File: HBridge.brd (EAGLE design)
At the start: 59.7 x 53.3 mm, 51 parts, among them IC1 74LS08D, IC2 A4954, J1 Inputs, J11 PWM mode, J12 Fixed mode, J13 Ground, J14 5V, J15 Digital_8_13, J16 Analog, J17 Digital_0_7, J4 PWM mode, J5 Fixed mode, J6 Power, J7 Output A, J8 Output B

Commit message: foo
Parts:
- moved J1 2.54 mm to (38.1, 36.8)
- moved C4 1.91 mm to (34.9, 21.6)
- moved R8 1.91 mm to (34.9, 19.7)
- moved R3 0.63 mm to (34.9, 23.5)
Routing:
- net IN4: track 18.3 -> 20.9 mm
- net PWM34: track 28.7 -> 29.8 mm
- net PWM12: track 31.7 -> 32.7 mm
- net IN2: track 24.1 -> 25.2 mm
- net IN1: track 23.6 -> 24.6 mm
- net REF_PWM_12: track 2.41 -> 3.20 mm
- net N$19: track 3.81 -> 4.45 mm

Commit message: foo
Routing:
- net N$66: track 11.4 -> 9.24 mm
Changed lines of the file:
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@@
 <wire x1="32.7025" y1="35.4965" x2="32.385" y2="35.814" width="0.4064" layer="1"/>
 <wire x1="32.385" y1="35.814" x2="32.385" y2="37.465" width="0.4064" layer="1"/>
-<wire x1="32.7025" y1="34.6075" x2="32.7025" y2="32.7025" width="0.3048" layer="16"/>
-<wire x1="32.7025" y1="32.7025" x2="31.75" y2="31.75" width="0.3048" layer="16"/>
-<wire x1="31.75" y1="31.75" x2="30.48" y2="31.75" width="0.3048" layer="16"/>
+<wire x1="32.7025" y1="34.6075" x2="32.7025" y2="32.7025" width="0.4064" layer="16"/>
+<wire x1="32.7025" y1="32.7025" x2="31.75" y2="31.75" width="0.4064" layer="16"/>
+<wire x1="31.75" y1="31.75" x2="30.48" y2="31.75" width="0.4064" layer="16"/>
 </signal>
 <signal name="N$17">
@@
 <wire x1="18.415" y1="34.29" x2="19.685" y2="35.56" width="0.4064" layer="1"/>
 <via x="19.685" y="35.56" extent="1-16" drill="0.4"/>
-<wire x1="38.1" y1="34.29" x2="34.29" y2="38.1" width="0.2032" layer="16"/>
-<wire x1="34.29" y1="38.1" x2="22.225" y2="38.1" width="0.2032" layer="16"/>
-<wire x1="22.225" y1="38.1" x2="19.685" y2="35.56" width="0.2032" layer="16"/>
+<wire x1="38.1" y1="34.29" x2="34.29" y2="38.1" width="0.4064" layer="16"/>
+<wire x1="31.115" y1="38.1" x2="27.305" y2="38.1" width="0.2032" layer="16"/>
+<wire x1="19.685" y1="35.56" x2="22.225" y2="38.1" width="0.4064" layer="16"/>
+<wire x1="22.225" y1="38.1" x2="27.305" y2="38.1" width="0.4064" layer="16"/>
+<wire x1="31.115" y1="38.1" x2="34.29" y2="38.1" width="0.4064" layer="16"/>
 </signal>
 <signal name="IN1">
@@
 <wire x1="22.86" y1="41.402" x2="32.258" y2="41.402" width="0.4064" layer="1"/>
 <wire x1="32.258" y1="41.402" x2="33.655" y2="40.005" width="0.4064" layer="1"/>
-<wire x1="38.1" y1="41.91" x2="40.64" y2="41.91" width="0.4064" layer="1"/>
+<wire x1="38.1" y1="41.91" x2="40.64" y2="41.91" width="0.8128" layer="1"/>
 <wire x1="48.26" y1="41.91" x2="50.8" y2="41.91" width="0.2032" layer="1"/>
 <wire x1="50.8" y1="41.91" x2="53.34" y2="41.91" width="0.4064" layer="1"/>
 <wire x1="53.34" y1="41.91" x2="55.88" y2="41.91" width="0.4064" layer="1"/>
-<wire x1="55.88" y1="41.91" x2="48.26" y2="41.91" width="0.4064" layer="1"/>
-<wire x1="48.26" y1="41.91" x2="45.72" y2="41.91" width="0.4064" layer="1"/>
-<wire x1="45.72" y1="41.91" x2="43.18" y2="41.91" width="0.4064" layer="1"/>
-<wire x1="43.18" y1="41.91" x2="40.64" y2="41.91" width="0.4064" layer="1"/>
+<wire x1="55.88" y1="41.91" x2="48.26" y2="41.91" width="0.8128" layer="1"/>
+<wire x1="48.26" y1="41.91" x2="45.72" y2="41.91" width="0.8128" layer="1"/>
+<wire x1="45.72" y1="41.91" x2="43.18" y2="41.91" width="0.8128" layer="1"/>
+<wire x1="43.18" y1="41.91" x2="40.64" y2="41.91" width="0.8128" layer="1"/>
 <wire x1="50.8" y1="41.91" x2="52.07" y2="40.64" width="0.4064" layer="16"/>
 <wire x1="53.34" y1="41.91" x2="52.07" y2="40.64" width="0.4064" layer="16"/>
@@
 <wire x1="25.4" y1="18.542" x2="25.273" y2="19.685" width="0.4064" layer="1"/>
 <via x="25.273" y="19.685" extent="1-16" drill="0.4"/>
-<wire x1="25.273" y1="19.685" x2="23.876" y2="21.082" width="0.4064" layer="16"/>
-<wire x1="23.876" y1="21.082" x2="23.876" y2="24.384" width="0.4064" layer="16"/>
-<wire x1="27.94" y1="26.67" x2="26.162" y2="26.67" width="0.4064" layer="16"/>
-<wire x1="26.162" y1="26.67" x2="23.876" y2="24.384" width="0.4064" layer="16"/>
+<wire x1="25.273" y1="19.685" x2="25.273" y2="24.003" width="0.4064" layer="16"/>
+<wire x1="25.273" y1="24.003" x2="27.94" y2="26.67" width="0.4064" layer="16"/>
 </signal>
 <signal name="N$67">

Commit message: foo
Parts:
- removed C9: 100nF, freetronics:0603
- removed J10, J9: (no value), freetronics-luke:HEADER_1X02
- removed J11: PWM mode, freetronics-luke:HEADER_1X02
- removed J12: Fixed mode, freetronics-luke:HEADER_1X02
- removed J13: Ground, freetronics-master-v1:1X08
- removed J14: 5V, freetronics-master-v1:1X08
- removed J15: Digital_8_13, freetronics:1X08
- removed J16: Analog, freetronics:1X06
- removed J17: Digital_0_7, freetronics:1X08
- removed R10, R8, R9: 1k, freetronics-master-v1:0603
- removed R11, R12: 0.25R 1W, rcl:R2010
- removed R13: 2K2, freetronics:0603
- removed R14: 10K, freetronics:0603
- removed S2: SWITCH, freetronics:TACTILE_SWITCH_SMD
- added JP2: +5V, SparkFun:1X07
- added JP3: (no value), freetronics-master-v1:1X02
- added RN1, RN2: 1K, freetronics-master-v1:CAY16
- added SJ1: Ch1 Fixed Current Select, freetronics-master-v1:SJ_2
- added SJ2: Ch2 Fixed Current Select, freetronics-master-v1:SJ_2
- added SJ3: Ch1 Fixed/PWM select, freetronics-master-v1:SJ_2
- added SJ4: Ch2 Fixed/PWM select, freetronics-master-v1:SJ_2
- C3: value 100 uF -> 100nF; device rcl:E3,5-8 -> freetronics-master-v1:0603
- C5: value 100nF -> 100 uF; device freetronics-master-v1:0603 -> freetronics-master-v1:PANASONIC_E
- IC1: value 74LS08D -> 74HC08D
- J1: value Inputs -> In 3/4; device freetronics-master-v1:1X08 -> freetronics-master-v1:1X04
- J2: value (none) -> Power; device freetronics-luke:HEADER_1X02 -> con-wago-508:W237-132
- J3: value (none) -> In 1/2; device freetronics-luke:HEADER_1X02 -> freetronics-master-v1:1X04
- J4: value PWM mode -> Output A; device freetronics-luke:HEADER_1X02 -> con-wago-508:W237-132
- J5: value Fixed mode -> Output B; device freetronics-luke:HEADER_1X02 -> con-wago-508:W237-132
- J6: value Power -> Digital_8_13; device con-wago-508:W237-132 -> freetronics:1X08
- J7: value Output A -> Analog; device con-wago-508:W237-132 -> freetronics:1X06
- J8: value Output B -> Digital_0_7; device con-wago-508:W237-132 -> freetronics:1X08
- JP1: value SWITCH -> Gnd; device freetronics:1X01 -> SparkFun:1X07
- R1: value 1k -> 2K2
- R2: value 2k2 -> 2K2
- R3, R4: value 1k -> 10k
- R5, R6: value 1k -> 0.25R 1W; device freetronics-master-v1:0603 -> rcl:R2010
- R7: value 2k2 -> 2K2; device freetronics-master-v1:0603 -> freetronics:0603
- moved J8 57.5 mm to (54.6, 50.8), turned to 180 degrees
- moved JP1 56.3 mm to (55.9, 11.4), turned to 180 degrees
- moved LED1 47.3 mm to (12.7, 50.5), turned to 90 degrees
- moved C8 44.4 mm to (11.0, 47.5)
- moved S1 43.3 mm to (5.71, 49.0), turned to 0 degrees
- moved J7 40.5 mm to (41.9, 2.54), turned to 0 degrees
- moved C5 36.8 mm to (8.70, 41.1), turned to 0 degrees
- moved R7 35.8 mm to (11.0, 50.5)
- moved C3 35.5 mm to (35.9, 36.2)
- moved J5 34.3 mm to (8.89, 6.35), turned to 270 degrees
- moved R5 31.4 mm to (18.4, 5.08)
- moved J6 28.0 mm to (32.8, 50.8), turned to 180 degrees
- moved J4 25.2 mm to (8.89, 16.5)
- moved C6 23.6 mm to (31.1, 19.4), turned to 0 degrees
- moved J2 22.9 mm to (8.89, 30.5)
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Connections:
- removed net N$249: JP1.1, R14.2, S2.3, S2.4
- removed net N$66: J10.2, R7.1
- removed net N$67: J10.1, J12.1, J9.1, R10.2
- removed net N$68: J9.2, R6.1
- removed net N$69: C5.1, J11.2, R9.2
- removed net N$83: C4.1, R8.2, R9.1
- new net N$1: RN2.4, SJ2.2, SJ4.3
- new net N$2: C4.1, RN2.2, SJ4.1
- new net N$20: RN2.6, SJ2.3
- new net N$3: C3.1, RN2.7, RN2.8
- new net N$4: R1.1, SJ1.1
- net +5V: now also JP2.1, JP2.2, JP2.3, JP2.4, JP2.5, JP2.6, JP2.7, RN1.3, RN2.3; no longer C9.1, J14.1, J14.2, J14.3, J14.4, J14.5, J14.6, J14.7, J14.8, R6.2, R7.2, S2.1, S2.2
- net A0: now also J7.1; no longer J16.1
- net A1: now also J7.2; no longer J16.2
- net A2: now also J7.3; no longer J16.3
- net A3: now also J7.4; no longer J16.4
- net A4: now also J7.5; no longer J16.5
- net A5: now also J7.6; no longer J16.6
- net AREF: now also J6.8; no longer J15.8
- net D0_RX: now also J8.1; no longer J17.1
- net D10: now also J6.3; no longer J15.3
- net D11_MOSI: now also J6.4; no longer J15.4
- net D12_MISO: now also J6.5; no longer J15.5
- net D13_SCK: now also J6.6; no longer J15.6
- net D1_TX: now also J8.2; no longer J17.2
- net D2: now also J8.3; no longer J17.3
- net D3: now also J8.4; no longer J17.4
- net D4: now also J8.5; no longer J17.5
- net D5: now also J8.6; no longer J17.6
- net D6: now also J8.7; no longer J17.7
- net D7: now also J8.8; no longer J17.8
- net D8: now also J6.1; no longer J15.1
- net D9: now also J6.2; no longer J15.2
- net GND: now also C3.2, C5.-, J2.2, J6.7, JP1.1, JP1.2, JP1.3, JP1.4, JP1.5, JP1.6, JP1.7, R3.1, R4.1, R6.1, R7.2, RN1.5, RN2.5; no longer C3.-, C5.2, C9.2, J13.1, J13.2, J13.3, J13.4, J13.5, J13.6, J13.7, J13.8, J15.7, J6.2, R10.1, R11.1, R12.1, R13.2, R14.1
- net IN1: now also J3.1; no longer J1.1
- net IN2: now also J3.2; no longer J1.2
- net IN3: now also J1.1; no longer J1.3
- net IN4: now also J1.2; no longer J1.4
- net N$10: now also J4.2; no longer J7.2
- net N$11: now also J5.1; no longer J8.1
- net N$12: now also J5.2; no longer J8.2
- net N$13: now also R5.2; no longer R11.2
- net N$14: now also R6.2; no longer R12.2
- net N$15: now also RN1.6, SJ1.3; no longer J3.2, R2.1
- net N$16: now also RN1.4, SJ1.2, SJ3.3; no longer J2.1, J3.1, J5.1, R5.2
- net N$17: now also R2.1, SJ2.1; no longer J2.2, R1.1
- net N$18: now also RN1.2, SJ3.1; no longer J4.2, R4.2
- net N$19: now also RN1.7, RN1.8; no longer R3.2, R4.1
- net N$248: now also R7.1; no longer R13.1
- net N$9: now also J4.1; no longer J7.1
- net PWM12: now also J3.3, R3.2; no longer J1.5
- net PWM34: now also J1.3, R4.2; no longer J1.6
- net REF_PWM_12: now also J3.4, RN1.1; no longer J1.7, R3.1
- net REF_PWM_34: now also J1.4, RN2.1; no longer J1.8, R8.1
- net VBB: now also C5.+, J2.1, JP3.2; no longer C3.+, J6.1
- net VIN: now also JP3.1
- net VREF12: now also SJ3.2; no longer J4.1, J5.2
- net VREF34: now also SJ4.2; no longer J11.1, J12.2
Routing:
- net RESET: track 31.2 -> 78.9 mm
- net +5V: track 232.9 -> 188.2 mm, vias 2 -> 5
- net VBB: track 45.7 -> 86.9 mm, vias 2 -> 4
- net VREF34: track 12.7 -> 48.2 mm, vias 0 -> 2
- net N$20: track 0.00 -> 25.0 mm, vias 0 -> 2
- net IN3: track 16.9 -> 37.7 mm
- net N$5: track 32.3 -> 11.6 mm, vias 2 -> 0
- net N$67: track 18.1 -> 0.00 mm, vias 2 -> 0
- net N$8: track 20.9 -> 5.26 mm, vias 2 -> 0
- net N$1: track 0.00 -> 15.2 mm, vias 1 -> 2
- net N$7: track 17.1 -> 3.56 mm, vias 2 -> 0
- net N$18: track 10.8 -> 23.9 mm, vias 0 -> 4
- net N$69: track 12.3 -> 0.00 mm, vias 1 -> 0
- net N$2: track 0.00 -> 11.8 mm, vias 1 -> 0
- net N$68: track 11.7 -> 0.00 mm
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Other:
- outline, holes or cut-outs redrawn
- board text added: "+"
- board text added: "0.6A"
- board text added: "1.2A"
- board text added: "1A"
- board text added: "255 PWM="
- board text added: "2A max I"
- board text added: "40V MAX +VIN"
- board text added: "B1"
- board text added: "B2"
- board text added: "CH A"
- board text added: "CH B"
- board text added: "CURRENT LIMIT CONFIGURATION"
- board text added: "FIXED"
- board text added: "Motor VIN"
- board text added: "OUTPUT A"
- board text added: "OUTPUT B"
- board text added: "PWM"
- board text removed: "10K"
- board text removed: "IN1"
- board text removed: "IN2"
- board text removed: "IN3"
- board text removed: "IN4"
- board text removed: "J12"
- board text removed: "J13"
- board text removed: "J8"
- board text removed: "J9"
- board text removed: "ON=HIGH"
- board text removed: "OUT1"
- board text removed: "OUT2"
- board text removed: "OUT3"
- board text removed: "OUT4"
- board text removed: "PWM1/2"
- board text removed: "PWM3/4"
- board text removed: "REF PWM1/2"
- board text removed: "REF PWM3/4"
- board text removed: "REF1/2FIX"
- board text removed: "REF1/2PWM"
- board text removed: "SWITCH"
- board text removed: "V+"
- board text removed: "VCC"

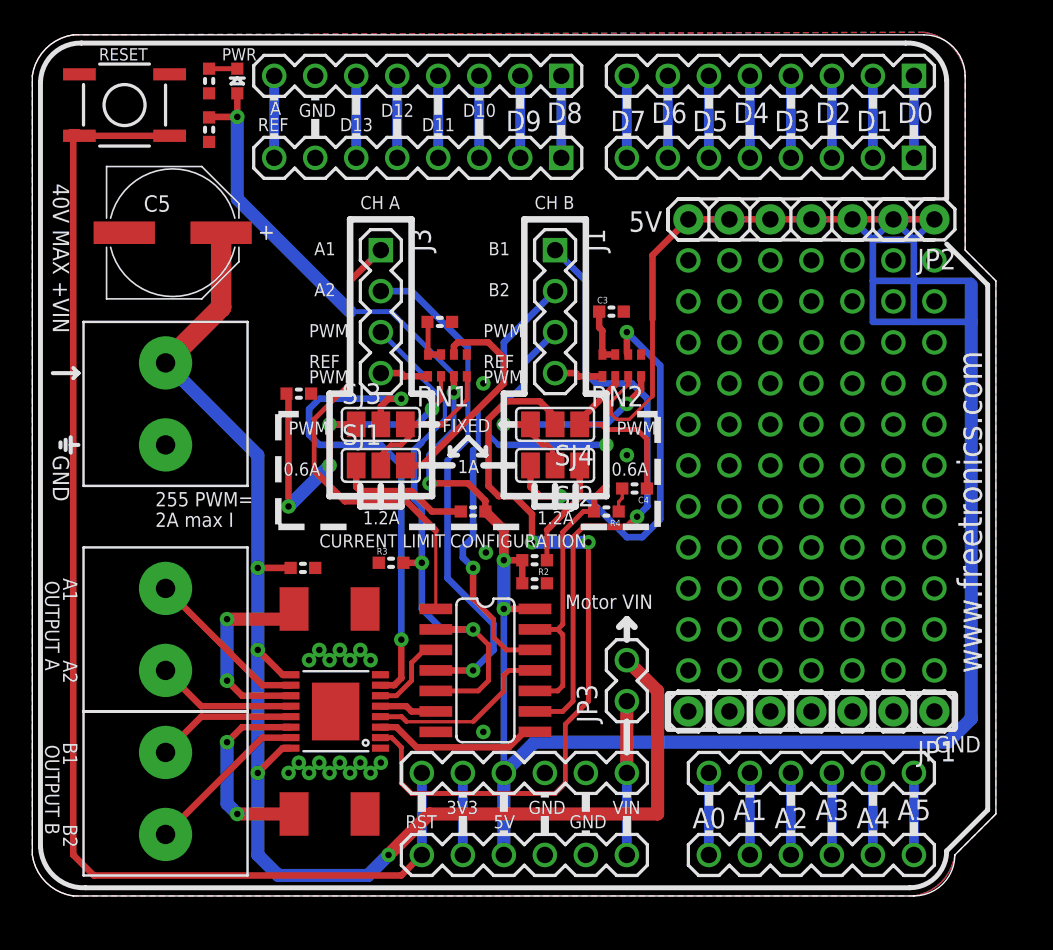
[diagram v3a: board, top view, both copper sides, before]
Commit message: Added ICSP header for R3
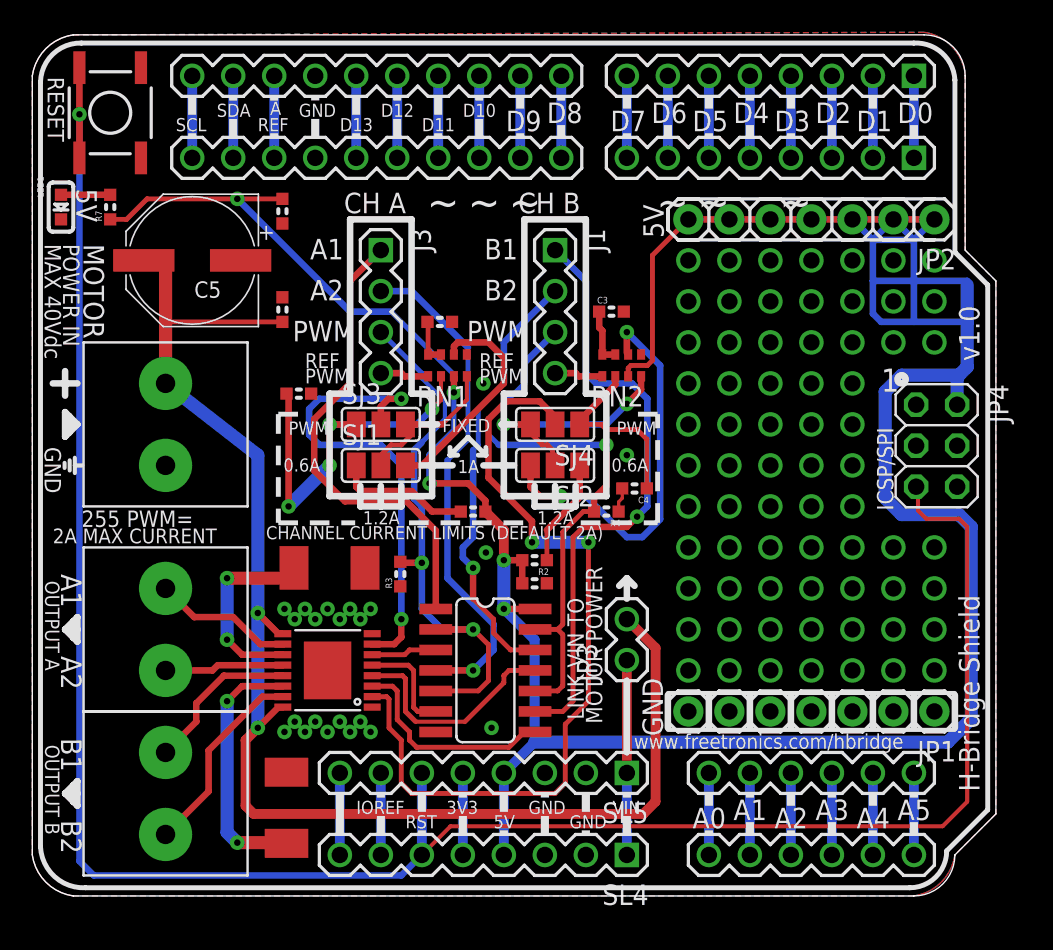
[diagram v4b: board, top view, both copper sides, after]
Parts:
- removed POWER, SLP: Power, freetronics:1X06
- added JP4: (no value), freetronics-master-v1:2X03
- added SL4, SL5: Digital_0_7, freetronics:1X08
- J6, SL1: device freetronics:1X08 -> freetronics-original:1X10
- moved C7 16.1 mm to (15.5, 36.3), turned to 90 degrees
- moved LED1 13.4 mm to (1.78, 42.7), turned to 270 degrees
- moved R7 9.93 mm to (4.83, 42.7), turned to 90 degrees
- moved C8 6.79 mm to (15.5, 42.4)
- moved R5 2.69 mm to (15.7, 5.46), turned to 270 degrees
- moved IC2 2.59 mm to (18.3, 14.0)
- moved JP3 2.54 mm to (36.8, 14.6)
- moved R6 2.54 mm to (18.4, 20.3)
- moved C5 2.10 mm to (9.91, 39.4), turned to 180 degrees
- moved J2 1.27 mm to (8.89, 29.2)
- moved S1 1.01 mm to (4.83, 48.5), turned to 270 degrees
- moved R3 0.90 mm to (22.8, 19.9), turned to 90 degrees
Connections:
- net D11_MOSI renamed D11
- net D12_MISO renamed D12
- net D13_SCK renamed D13
- removed net N$248: LED1.C, R7.1
- new net IOREF: SL4.7, SL5.7
- new net MISO: JP4.1
- new net MOSI: JP4.4
- new net N$22: LED1.A, R7.2
- new net SCK: JP4.3
- new net SCL: J6.10, SL1.10
- new net SDA: J6.9, SL1.9
- new net UNUSED: SL4.8, SL5.8
- net +5V: now also JP4.2, R7.1, SL4.4, SL5.4; no longer LED1.A, POWER.3, SLP.3
- net 3V3: now also SL4.5, SL5.5; no longer POWER.2, SLP.2
- net GND: now also JP4.6, LED1.C, SL4.2, SL4.3, SL5.2, SL5.3; no longer POWER.4, POWER.5, R7.2, SLP.4, SLP.5
- net RESET: now also JP4.5, SL4.6, SL5.6; no longer POWER.1, SLP.1
- net VIN: now also SL4.1, SL5.1; no longer POWER.6, SLP.6
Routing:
- net RESET: track 78.9 -> 136.2 mm, vias 0 -> 1
- net +5V: track 188.2 -> 193.4 mm
- net UNUSED: track 0.00 -> 5.08 mm
- net IOREF: track 0.00 -> 5.08 mm
- net SDA: track 0.00 -> 5.08 mm
- net SCL: track 0.00 -> 5.08 mm
- net N$13: track 12.6 -> 15.9 mm
- net N$22: track 0.00 -> 3.05 mm, vias 1 -> 0
- net N$7: track 3.56 -> 6.46 mm
- net N$6: track 10.5 -> 13.4 mm
- net VIN: track 9.52 -> 12.1 mm
- net N$5: track 11.6 -> 14.0 mm
- net VREF34: track 48.2 -> 50.5 mm
- net N$12: track 10.3 -> 12.3 mm
- net VREF12: track 31.3 -> 29.3 mm
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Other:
- board text added: "1"
- board text added: "2A MAX CURRENT"
- board text added: "CHANNEL CURRENT LIMITS (DEFAULT 2A)"
- board text added: "H-Bridge Motor Controller"
- board text added: "H-Bridge Shield"
- board text added: "ICSP/SPI"
- board text added: "IOREF"
- board text added: "LINK VIN TO"
- board text added: "MAX 40Vdc"
- board text added: "MOTOR"
- board text added: "MOTOR POWER"
- board text added: "POWER IN"
- board text added: "SCL"
- board text added: "SDA"
- board text added: "SKU: HBRIDGE"
- board text added: "V1.0"
- board text added: "v1.0"
- board text added: "www.freetronics.com/hbridge"
- board text added: "~"
- board text removed: "2A max I"
- board text removed: "40V MAX +VIN"
- board text removed: "CURRENT LIMIT CONFIGURATION"
- board text removed: "Motor VIN"
- board text removed: "PWR"
